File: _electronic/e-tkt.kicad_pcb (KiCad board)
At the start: 4 copper layers, 99.6 x 76.2 mm, 107 parts, among them J1 Conn_01x03_Pin, J2 Conn_01x03_Pin, J3 Conn_01x03_Pin

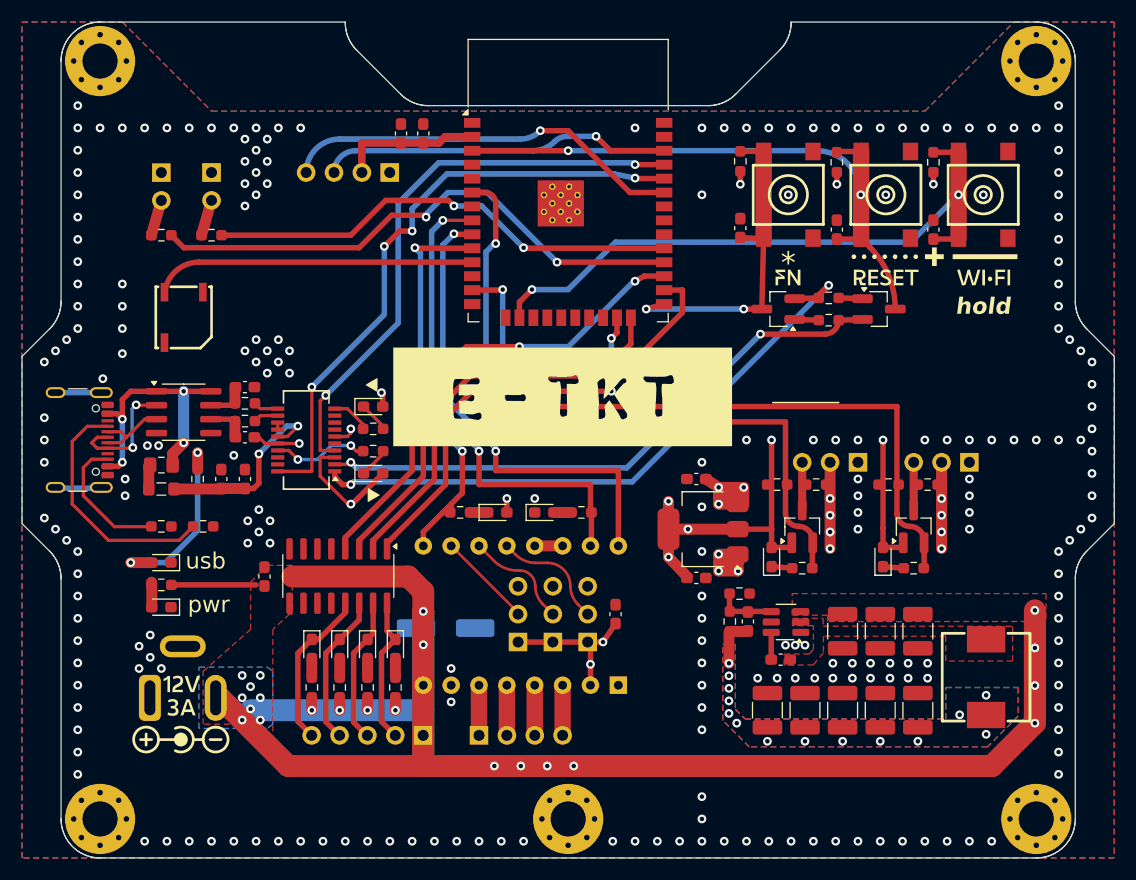
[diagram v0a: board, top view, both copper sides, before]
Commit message: Decluttering traces and Compactifying Part placement
many parts have been place in a compact format,
footprint layout optimized for function and visuals
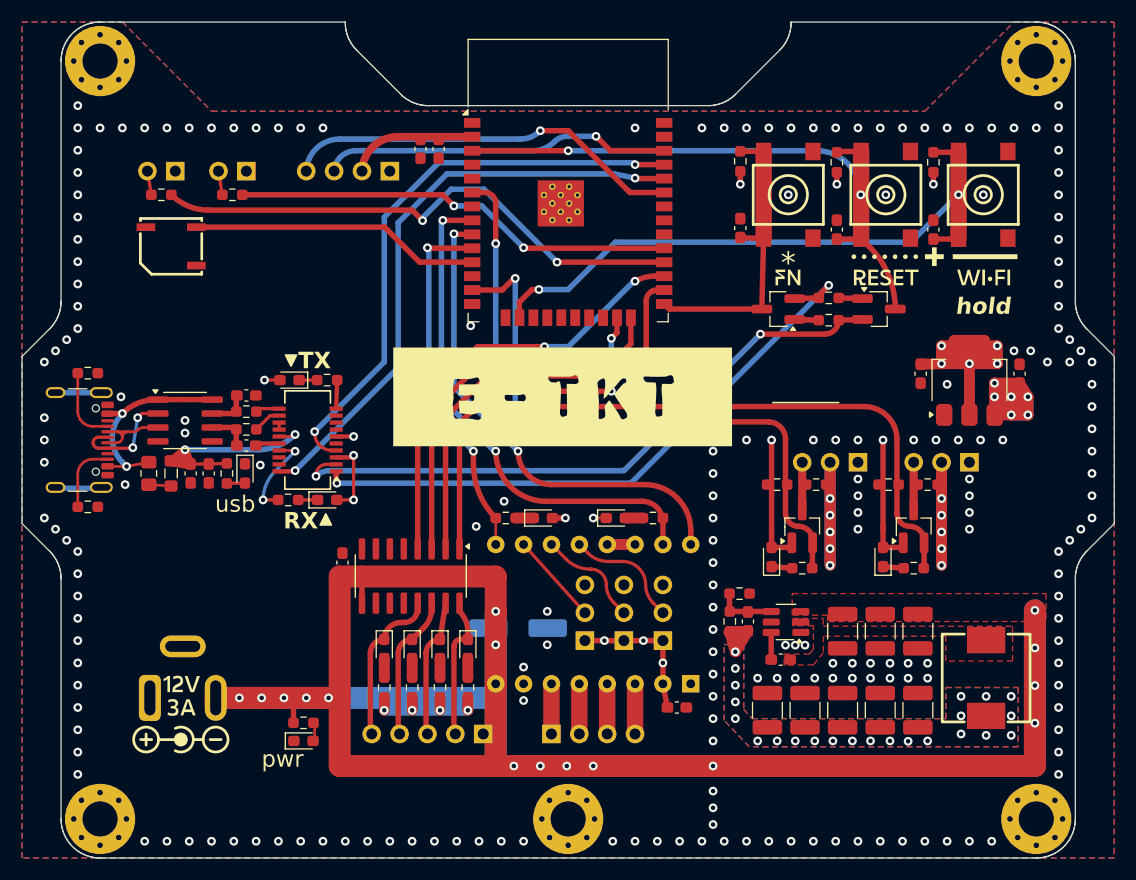
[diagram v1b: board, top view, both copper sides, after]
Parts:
- moved G*** 53.0 mm to (127.6, -208.0)
- moved C_POW1 31.0 mm to (219.5, -195.5), turned to 90 degrees
- moved U_POW2 27.8 mm to (214.9, -194.9), turned to 90 degrees
- moved C_POW2 27.7 mm to (210.4, -195.5), turned to -90 degrees
- moved R_POW6 18.1 mm to (154.2, -163.7), turned to 0 degrees
- moved D_POW2 17.8 mm to (154.2, -162.1), turned to 0 degrees
- moved R_USB1 17.5 mm to (134.5, -195.6)
- moved D_USB1 11.1 mm to (148.8, -186.4), turned to -90 degrees
- moved C_NEMA2 10.2 mm to (188.2, -165.1), turned to 180 degrees
- moved R_RX1 8.93 mm to (152.8, -184.0)
- moved D_TX1 7.99 mm to (152.9, -194.9), turned to 180 degrees
- moved C_STP1 7.22 mm to (157.7, -178.3)
- moved R_USB2 6.94 mm to (134.5, -183.4)
- moved J3 6.86 mm to (186.9, -171.2)
- moved A_NEMA1 6.61 mm to (189.5, -167.3)
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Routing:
- net +6V: track 31.5 -> 82.5 mm, vias 25 -> 39
- net +12V: track 226.5 -> 260.0 mm, vias 22 -> 20
- net Net-(D_USB1-A): track 17.6 -> 1.65 mm, vias 2 -> 0
- net Net-(J_USB1-CC1): track 22.4 -> 6.93 mm
- net GNDREF: track 23.1 -> 13.8 mm, vias 233 -> 205
- net Net-(J_USB1-CC2): track 12.5 -> 6.43 mm
- net IO4 ULN 2: track 45.1 -> 39.2 mm
- net Net-(F_USB1-Pad1): track 24.3 -> 19.0 mm, vias 4 -> 2
- net RTS: track 54.1 -> 58.4 mm
- net +3.3V: track 83.8 -> 87.4 mm, vias 13 -> 17
- net IO25 NEMA ENA: track 37.4 -> 33.8 mm
- net IO2 ULN 3: track 39.3 -> 35.8 mm
- net IO16 ULN 4: track 43.4 -> 40.0 mm
- net /MCU/IO26 BUZZER OUT: track 30.0 -> 26.7 mm
- net IO0 DFU: track 31.4 -> 28.3 mm, vias 2 -> 0
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- removed copper zone on B.Cu, net +12V
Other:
- board text added: "+"
- board text added: "2025/10/25"
- board text added: "NEMA17|STEPPER|28BYJ-48"
- board text added: "RX"
- board text added: "TX"
- board text added: "Vmot"
- board text removed: "2022/09/23"
- board text removed: "NEMA"
- board text removed: "STEPPER"
- board text removed: "VMOT"

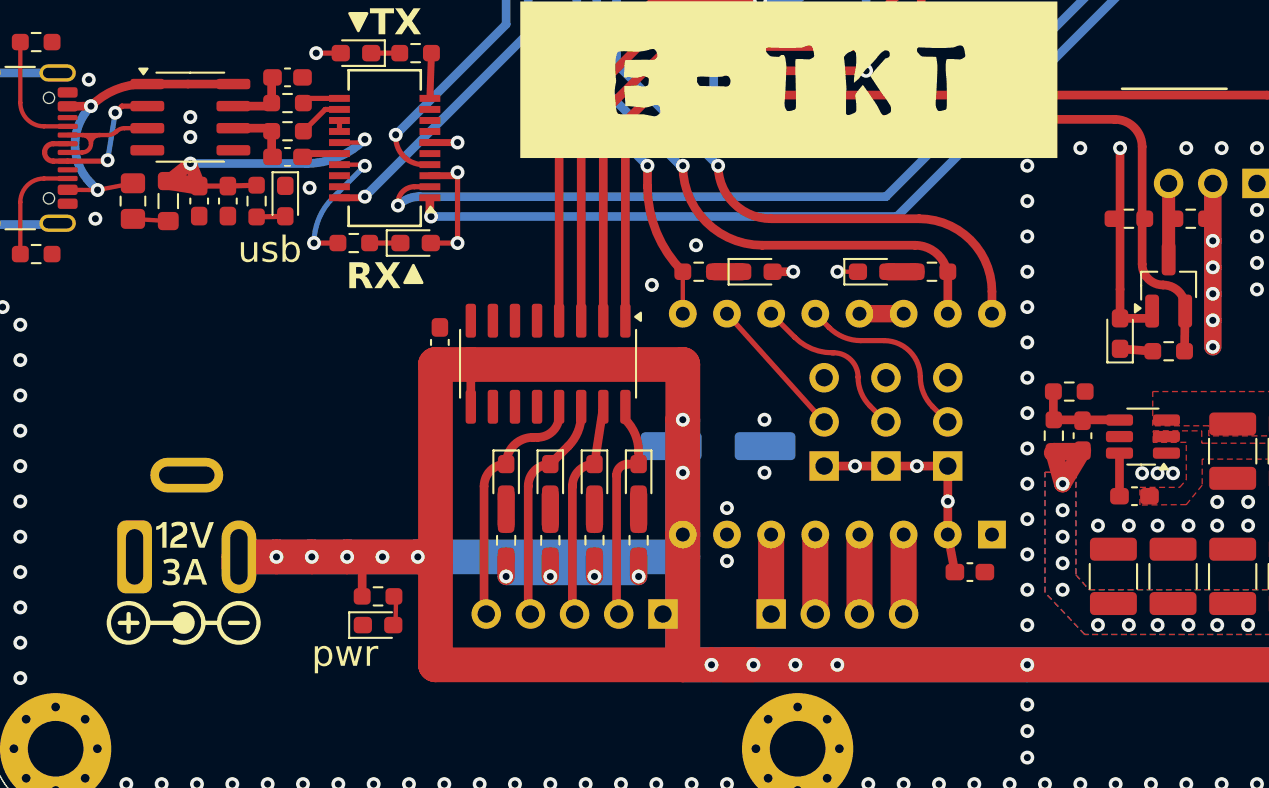
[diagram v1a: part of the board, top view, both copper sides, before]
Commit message: USB-C PD added
in parallel to DC jack, realized via HUSB237
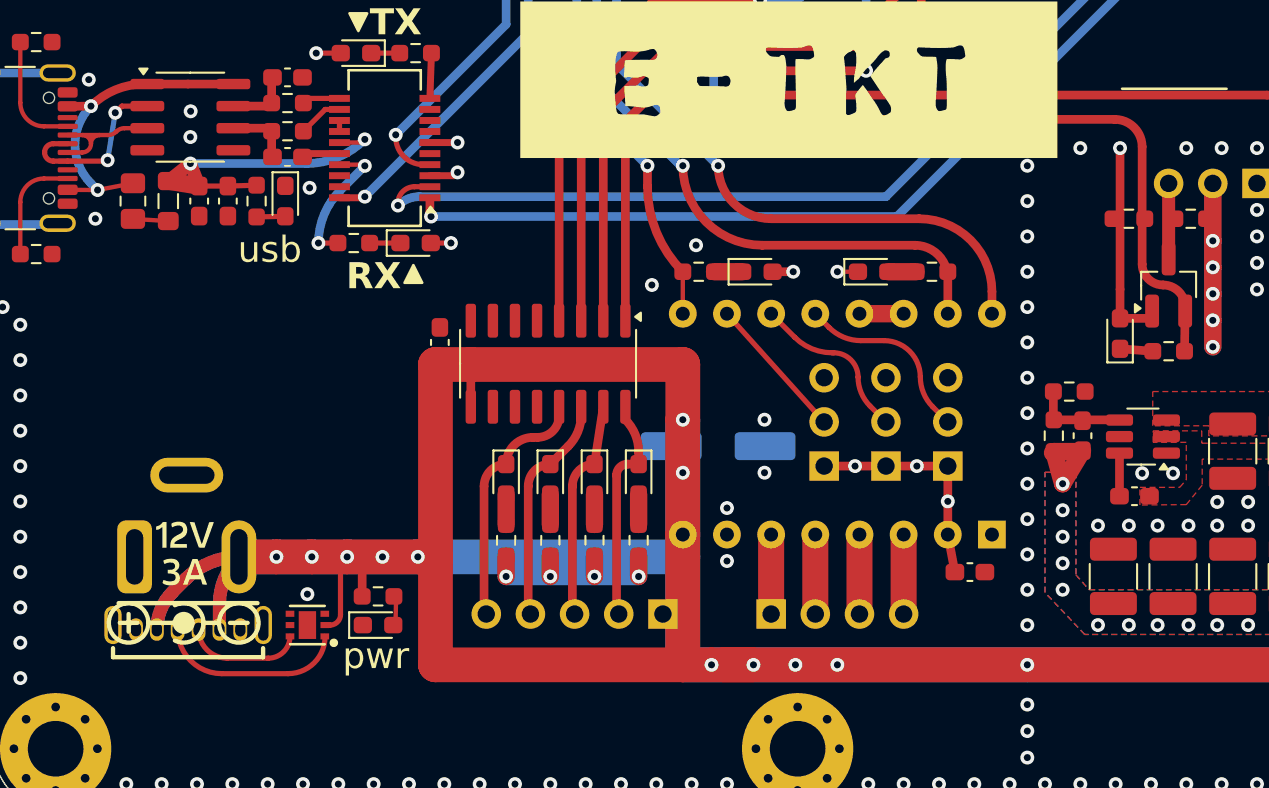
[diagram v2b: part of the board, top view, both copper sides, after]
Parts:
- added J4: USB_C_Receptacle_PowerOnly_6P, EASYEDA2KICAD:USB-C-TH_TYPE-C-6PLCH10.0-073, F.Cu at (143.3, -161.9)
- added U1: HUSB237-AA001-DN06R, EASYEDA2KICAD:TDFN-6_L2.0-W2.0-P0.65-TL-EP, F.Cu at (150.1, -162.1)
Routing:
- net +12V: track 260.0 -> 287.3 mm
- net Net-(J4-CC1): track 0.00 -> 11.0 mm
- net Net-(J4-CC2): track 0.00 -> 6.80 mm
- net +3.3V: track 87.4 -> 83.0 mm

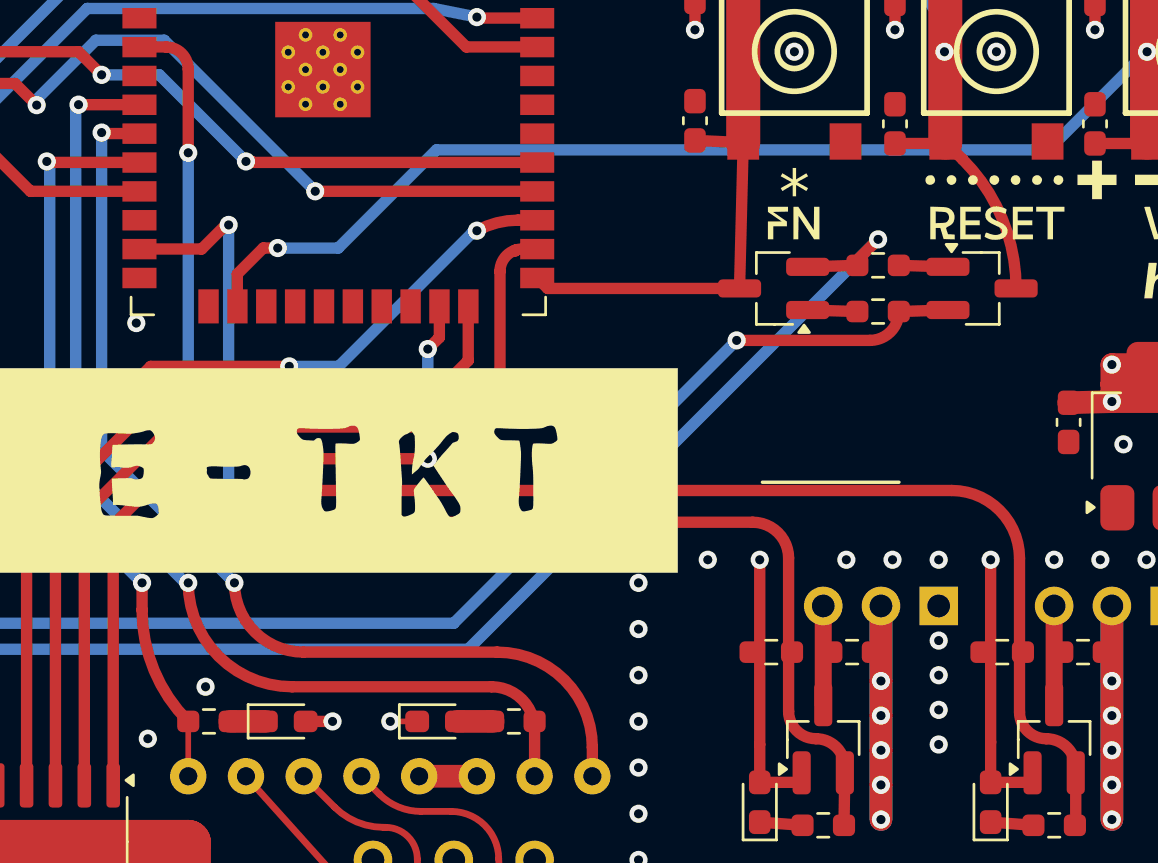
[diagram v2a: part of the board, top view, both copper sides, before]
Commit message: Updated USB-C PD layout and zoning
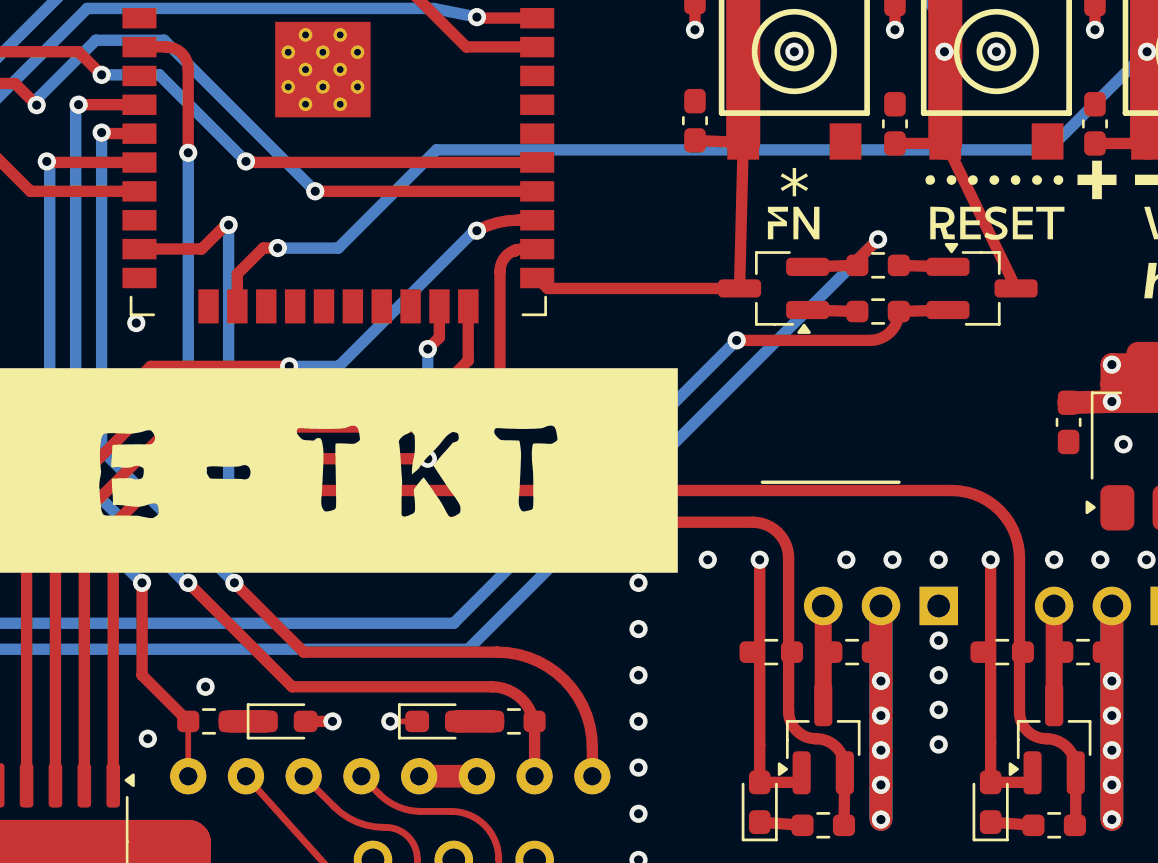
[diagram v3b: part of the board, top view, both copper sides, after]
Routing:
- net IO32 NEMA STEP: track 46.9 -> 46.4 mm

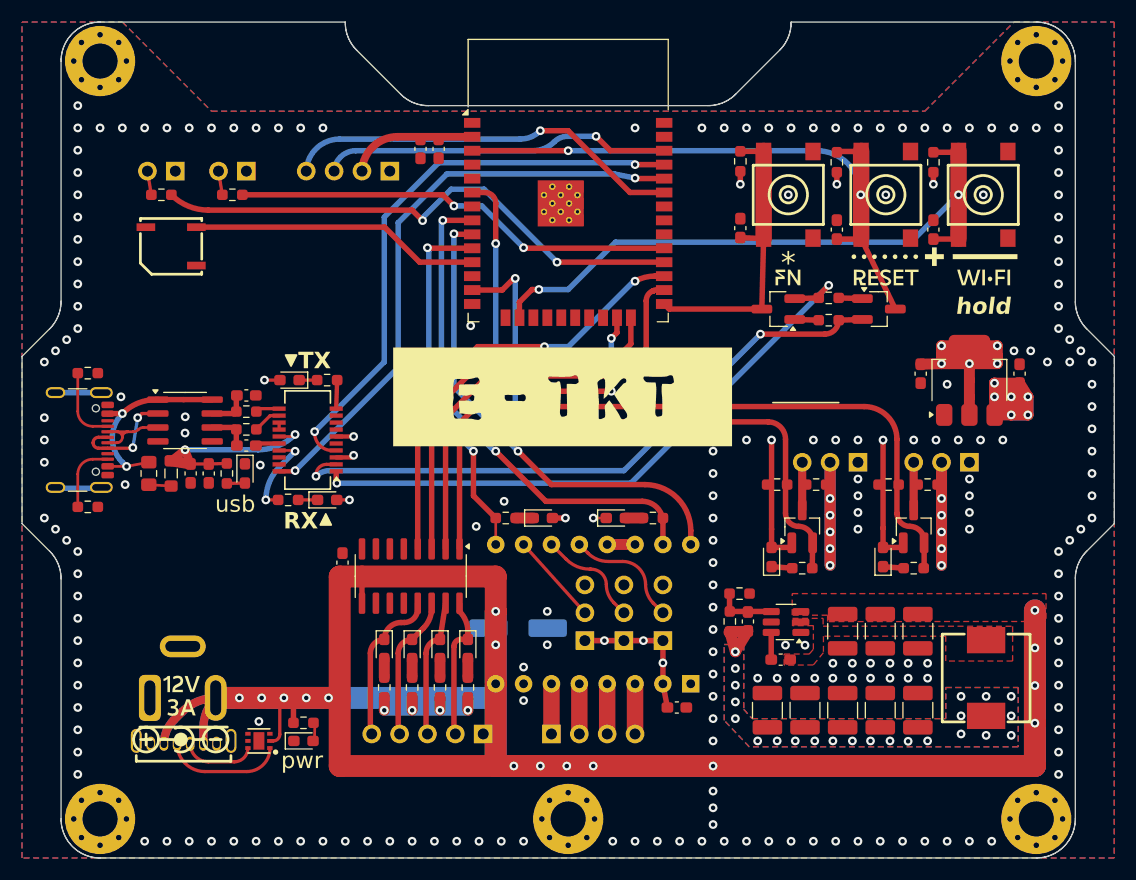
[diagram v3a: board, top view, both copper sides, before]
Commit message: Optimized alignment of USB-C socket
so that there is more tolerance for printed parts
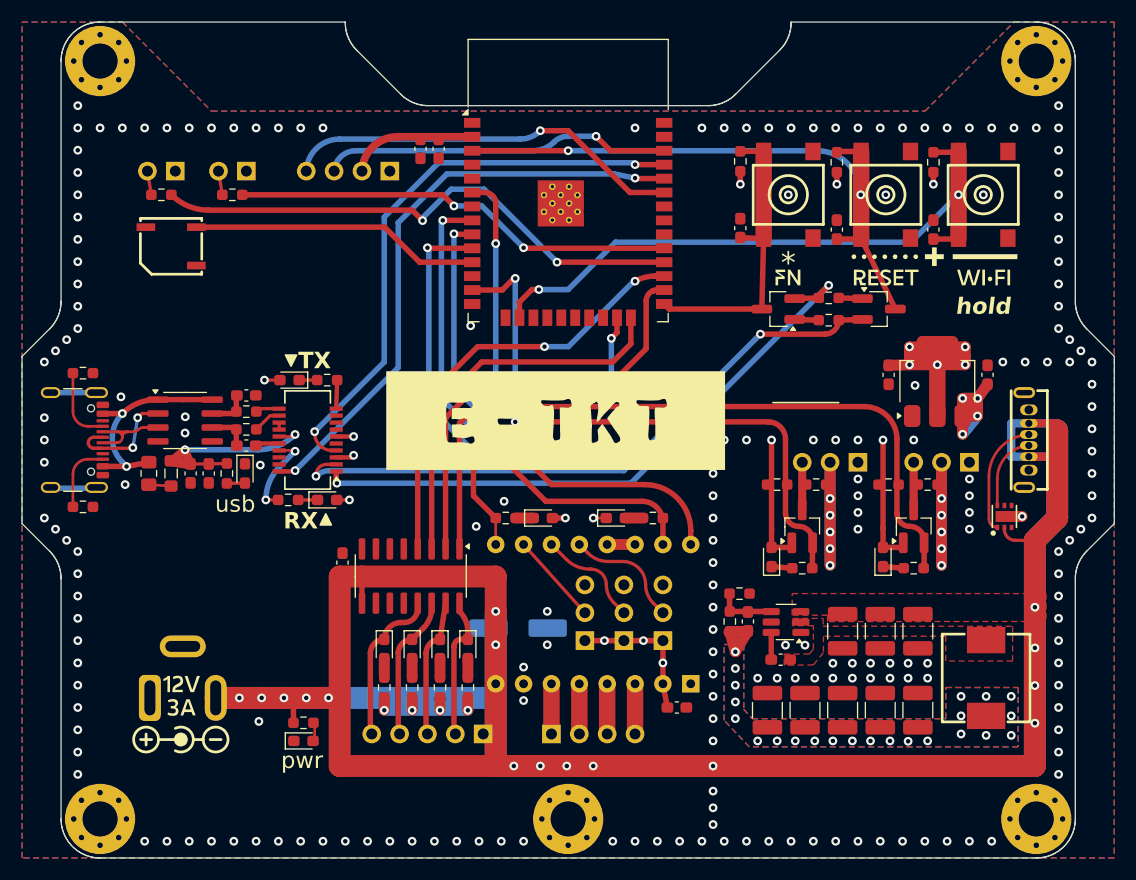
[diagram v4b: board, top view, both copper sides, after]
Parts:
- J4: footprint EASYEDA2KICAD:USB-C-TH_TYPE-C-6PLCH10.0-073 -> EASYEDA2KICAD:USB-C-TH_TYPE-604-T3-5A
- moved J4 81.6 mm to (220.1, -189.5), turned to -90 degrees
- moved U1 71.0 mm to (218.1, -182.5), turned to 90 degrees
- moved G*** 22.2 mm to (142.4, -201.0)
- moved C_POW1 2.92 mm to (216.5, -195.4)
- moved C_POW2 2.92 mm to (207.5, -195.4)
- moved U_POW2 2.92 mm to (212.0, -194.8)
- moved G*** 2.82 mm to (152.4, -217.0)
- moved G*** 2.25 mm to (177.2, -191.3)
- moved J_USB1 0.44 mm to (132.2, -189.5)
- moved R_USB1 0.44 mm to (134.1, -195.6)
- moved R_USB2 0.44 mm to (134.1, -183.4)
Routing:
- net +12V: track 287.3 -> 314.8 mm
- net +6V: track 82.5 -> 59.9 mm, vias 39 -> 37
- net GNDREF: track 13.8 -> 15.4 mm, vias 205 -> 202
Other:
- board text added: "3V3 Space"
- board text added: "DC space (obsolete?)"
- board text added: "DCDC space"
- board text added: "ESP32 space and via wiring overhead"
- board text added: "Level Shift Space"
- board text added: "Motor 1 space"
- board text added: "Provisional USB-C PD space"
- board text added: "USB FTDI Space"
- board text added: "theoretical Motor 2 space"
